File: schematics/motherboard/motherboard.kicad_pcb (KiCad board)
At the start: 2 copper layers, 75 x 43 mm, 2 parts, among them J1 BATTERY, U1 Raspberry_Pi_Pico

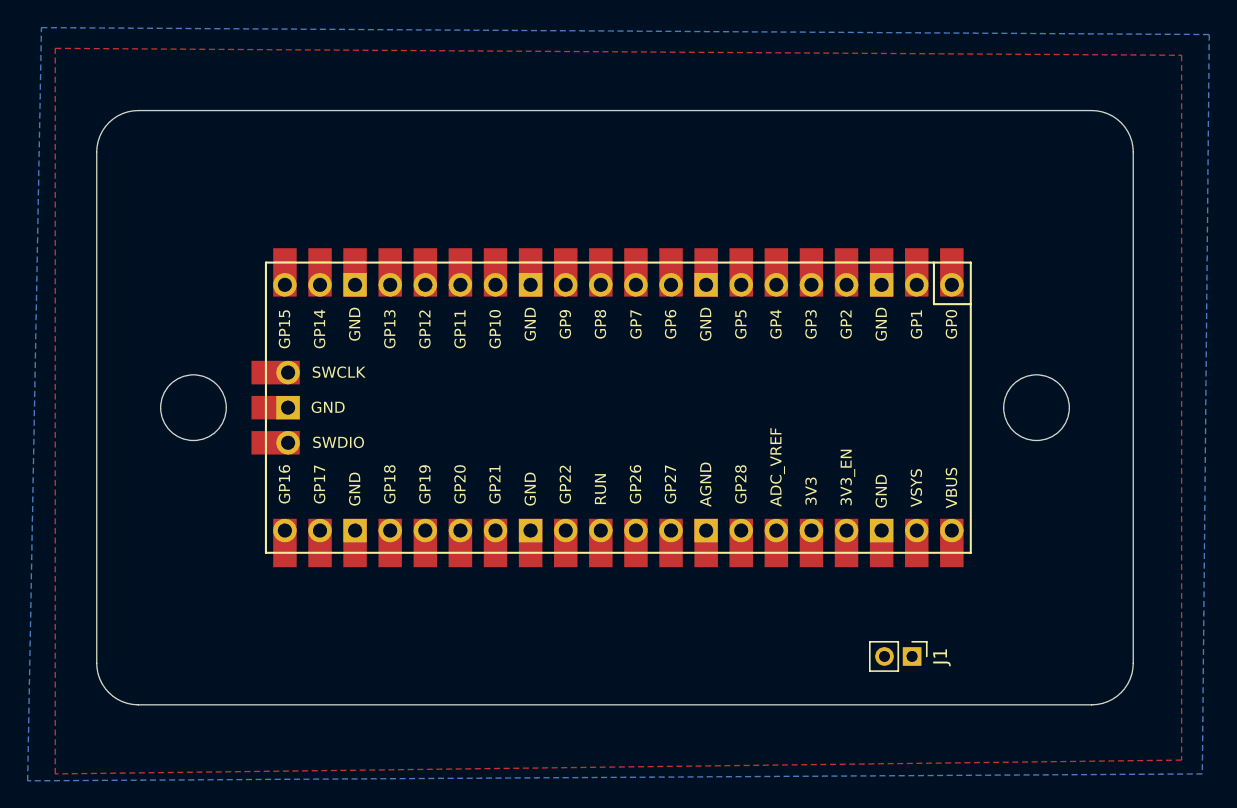
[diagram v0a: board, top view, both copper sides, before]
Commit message: Update fret_board, motherboard and strum_bar schematics
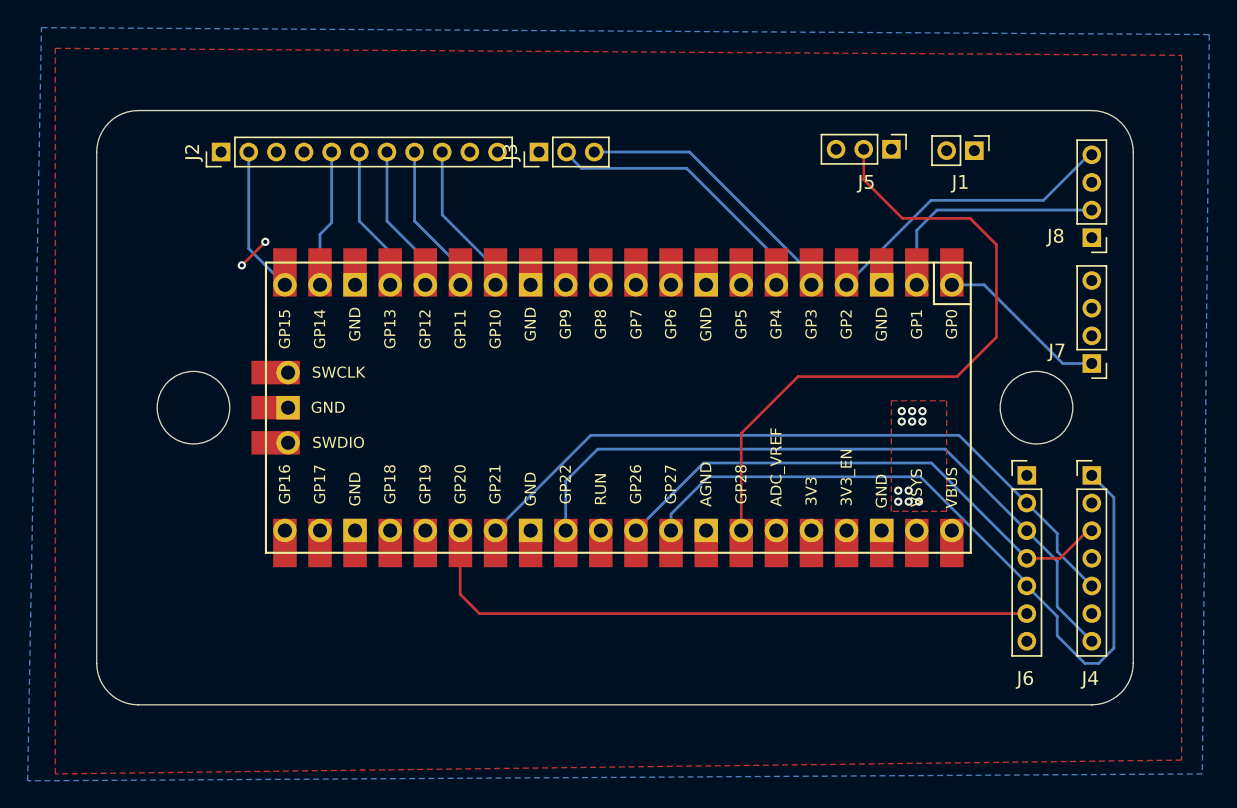
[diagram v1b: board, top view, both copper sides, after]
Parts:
- added J2: NECK, Connector_PinHeader_2.00mm:PinHeader_1x11_P2.00mm_Vertical, F.Cu at (168.0, 51.0)
- added J3: STRUM, Connector_PinHeader_2.00mm:PinHeader_1x03_P2.00mm_Vertical, F.Cu at (191.0, 51.0)
- added J4: DPAD_XBOX, Connector_PinHeader_2.00mm:PinHeader_1x07_P2.00mm_Vertical, F.Cu at (231.0, 74.4)
- added J5: WHAMMY, Connector_PinHeader_2.00mm:PinHeader_1x03_P2.00mm_Vertical, F.Cu at (216.5, 50.8)
- added J6: DPAD_PS2, Connector_PinHeader_2.00mm:PinHeader_1x07_P2.00mm_Vertical, F.Cu at (226.3, 74.4)
- added J7: PAIRING_BTN_XBOX, Connector_PinHeader_2.00mm:PinHeader_1x04_P2.00mm_Vertical, F.Cu at (231.0, 66.3)
- added J8: START_SELECT, Connector_PinHeader_2.00mm:PinHeader_1x04_P2.00mm_Vertical, F.Cu at (231.0, 57.2)
- moved J1 36.9 mm to (222.5, 50.9)
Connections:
- U1 pad 1: unconnected-(U1-GPIO0-Pad1) -> BTN_PAIRING
- U1 pad 14: unconnected-(U1-GPIO10-Pad14) -> FRET_ORANGE
- U1 pad 15: unconnected-(U1-GPIO11-Pad15) -> FRET_BLUE
- U1 pad 16: unconnected-(U1-GPIO12-Pad16) -> FRET_YELLOW
- U1 pad 17: unconnected-(U1-GPIO13-Pad17) -> FRET_RED
- U1 pad 19: unconnected-(U1-GPIO14-Pad19) -> FRET_GREEN
- U1 pad 2: unconnected-(U1-GPIO1-Pad2) -> BTN_START
- U1 pad 20: unconnected-(U1-GPIO15-Pad20) -> NECK_SLIDER
- U1 pad 26: unconnected-(U1-GPIO20-Pad26) -> PS2_LED
- U1 pad 27: unconnected-(U1-GPIO21-Pad27) -> DPAD_UP
- U1 pad 29: unconnected-(U1-GPIO22-Pad29) -> DPAD_DOWN
- U1 pad 31: unconnected-(U1-GPIO26_ADC0-Pad31) -> DPAD_LEFT
- U1 pad 32: unconnected-(U1-GPIO27_ADC1-Pad32) -> DPAD_RIGHT
- U1 pad 34: unconnected-(U1-GPIO28_ADC2-Pad34) -> WHAMMY
- U1 pad 4: unconnected-(U1-GPIO2-Pad4) -> BTN_SELECT
- U1 pad 5: unconnected-(U1-GPIO3-Pad5) -> STRUM_UP
- U1 pad 6: unconnected-(U1-GPIO4-Pad6) -> STRUM_DOWN
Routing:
- net DPAD_RIGHT: track 0.00 -> 54.5 mm
- net DPAD_UP: track 0.00 -> 51.3 mm
- net DPAD_DOWN: track 0.00 -> 50.3 mm
- net WHAMMY: track 0.00 -> 48.8 mm
- net PS2_LED: track 0.00 -> 46.2 mm
- net DPAD_LEFT: track 0.00 -> 38.7 mm
- net BTN_SELECT: track 0.00 -> 21.6 mm
- net STRUM_DOWN: track 0.00 -> 20.3 mm
- net STRUM_UP: track 0.00 -> 20.2 mm
- net BTN_START: track 0.00 -> 17.2 mm
- net BTN_PAIRING: track 0.00 -> 12.5 mm
- net FRET_ORANGE: track 0.00 -> 11.2 mm
- net FRET_BLUE: track 0.00 -> 11.0 mm
- net FRET_YELLOW: track 0.00 -> 10.8 mm
- net NECK_SLIDER: track 0.00 -> 10.7 mm
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- added copper zone on F.Cu, net VCC
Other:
- outline, holes or cut-outs redrawn

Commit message: Add battery sensing circuit and reverse polarity protection diode
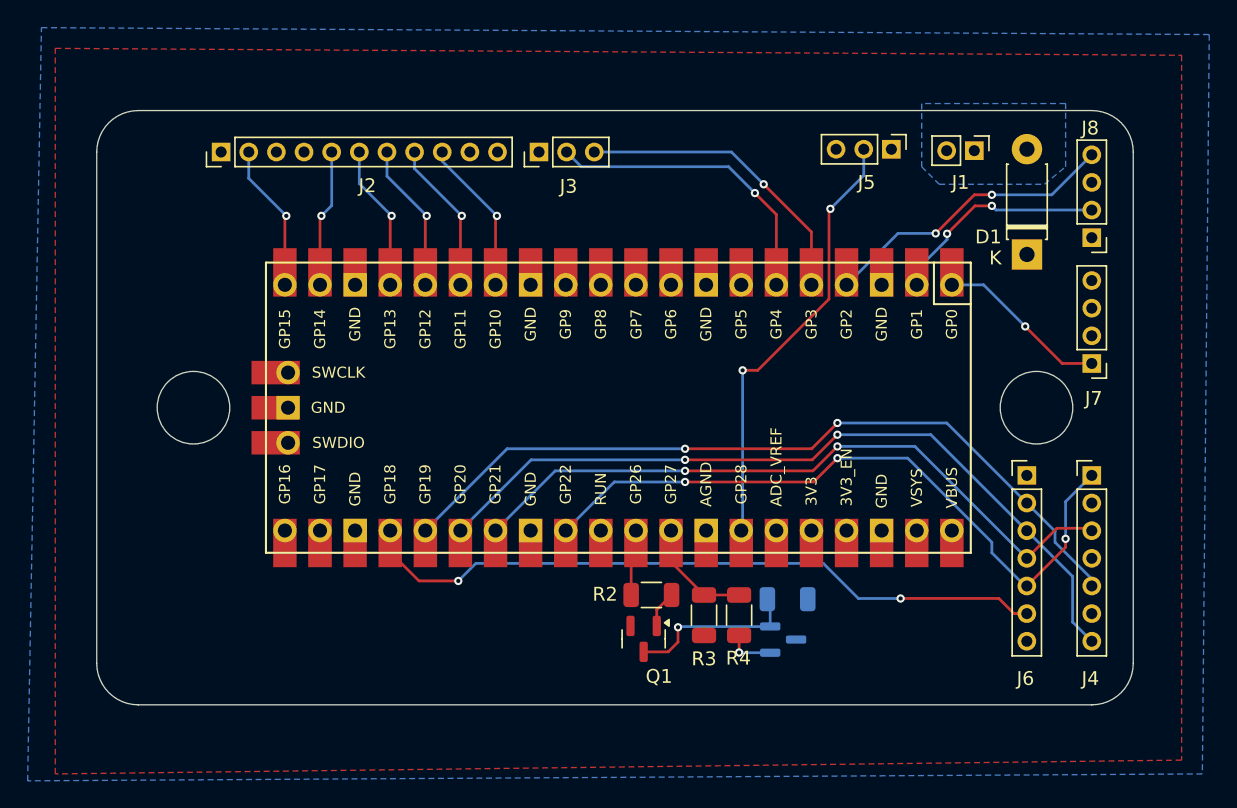
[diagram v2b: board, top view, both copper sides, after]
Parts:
- added D1: 1N5817, Diode_THT:D_DO-41_SOD81_P7.62mm_Horizontal, F.Cu at (226.3, 58.4)
- added Q1: BC847, Package_TO_SOT_SMD:SOT-23, F.Cu at (198.6, 86.2)
- added Q2: IRF5305, Package_TO_SOT_SMD:SOT-23, B.Cu at (208.7, 86.3)
- added R1: 100k, Resistor_SMD:R_1206_3216Metric, B.Cu at (209.0, 83.4)
- added R2: 100k, Resistor_SMD:R_1206_3216Metric, F.Cu at (199.1, 83.1)
- added R3: 100k, Resistor_SMD:R_1206_3216Metric, F.Cu at (205.5, 84.5)
- added R4: 330k, Resistor_SMD:R_1206_3216Metric, F.Cu at (202.9, 84.5)
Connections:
- J1 pad 1: VCC -> /VBAT
- U1 pad 24: unconnected-(U1-GPIO18-Pad24) -> PS2_LED
- U1 pad 25: unconnected-(U1-GPIO19-Pad25) -> DPAD_UP
- U1 pad 26: PS2_LED -> DPAD_DOWN
- U1 pad 27: DPAD_UP -> DPAD_LEFT
- U1 pad 29: DPAD_DOWN -> DPAD_RIGHT
- U1 pad 31: DPAD_LEFT -> VBAT_SENSE_SWITCH
- U1 pad 32: DPAD_RIGHT -> VBAT_SENSE
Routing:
- net WHAMMY: track 48.8 -> 31.9 mm, vias 0 -> 2
- net Net-(Q1-C): track 0.00 -> 12.6 mm, vias 0 -> 1
- net DPAD_LEFT: track 38.7 -> 50.0 mm, vias 0 -> 2
- net VBAT_SENSE: track 0.00 -> 8.19 mm
- net DPAD_DOWN: track 50.3 -> 56.7 mm, vias 0 -> 2
- net DPAD_UP: track 51.3 -> 57.1 mm, vias 0 -> 2
- net VBAT_SENSE_SWITCH: track 0.00 -> 4.81 mm
- net DPAD_RIGHT: track 54.5 -> 49.8 mm, vias 0 -> 3
- net PS2_LED: track 46.2 -> 50.5 mm, vias 0 -> 2
- net Net-(Q2-D): track 0.00 -> 3.49 mm, vias 0 -> 1
- net Net-(Q1-B): track 0.00 -> 2.68 mm
- net VCC: track 2.40 -> 0.00 mm, vias 13 -> 0
- net STRUM_DOWN: track 20.3 -> 22.1 mm, vias 0 -> 1
- net STRUM_UP: track 20.2 -> 21.9 mm, vias 0 -> 1
- net BTN_START: track 17.2 -> 16.0 mm, vias 0 -> 2
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- added copper zone on B.Cu, net /VBAT
- removed copper zone on F.Cu, net VCC

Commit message: Add silkscreen graphics to each schematic
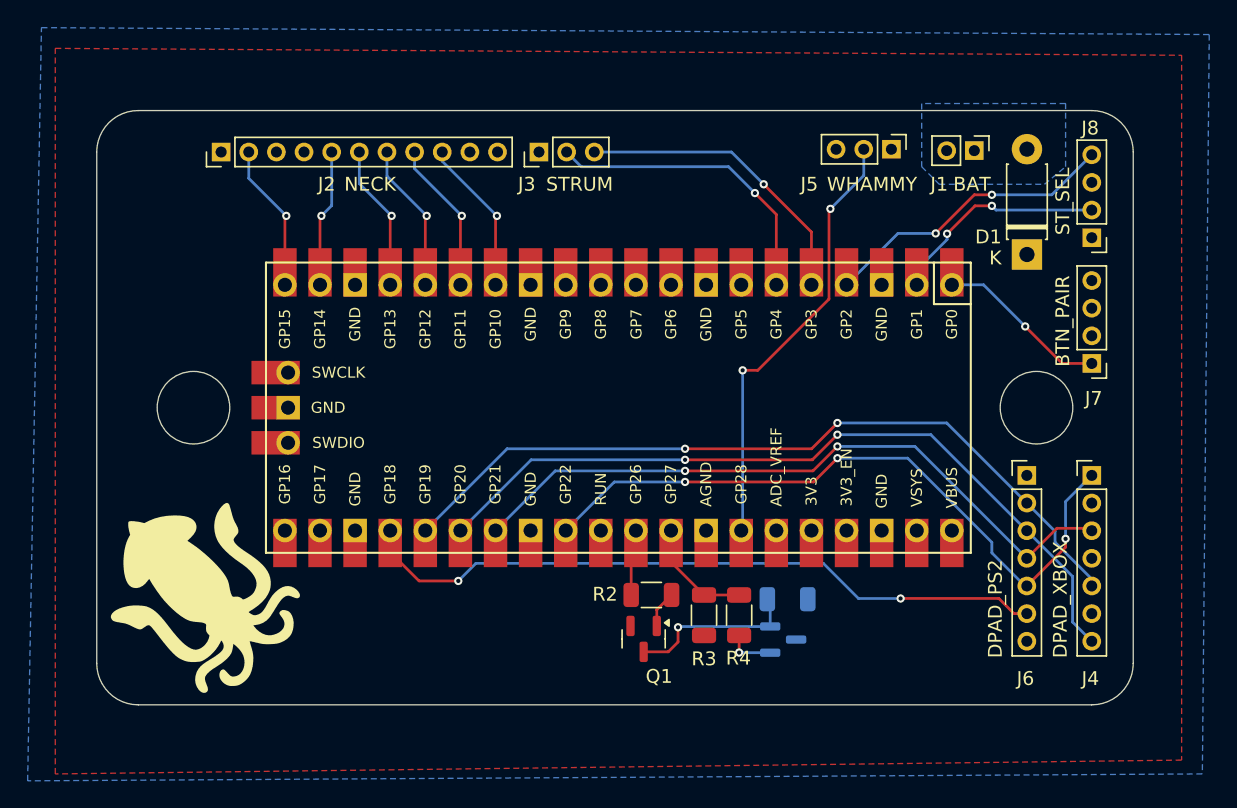
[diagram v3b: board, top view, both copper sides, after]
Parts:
- added G***: LOGO, LOGO, F.Cu at (166.9, 83.3)
- J1: value BATTERY -> BAT
- J8: value START_SELECT -> ST_SEL
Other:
- board text added: "BAT"
- board text added: "BTN_PAIR"
- board text added: "DPAD_PS2"
- board text added: "DPAD_XBOX"
- board text added: "NECK"
- board text added: "STRUM"
- board text added: "ST_SEL"
- board text added: "WHAMMY"

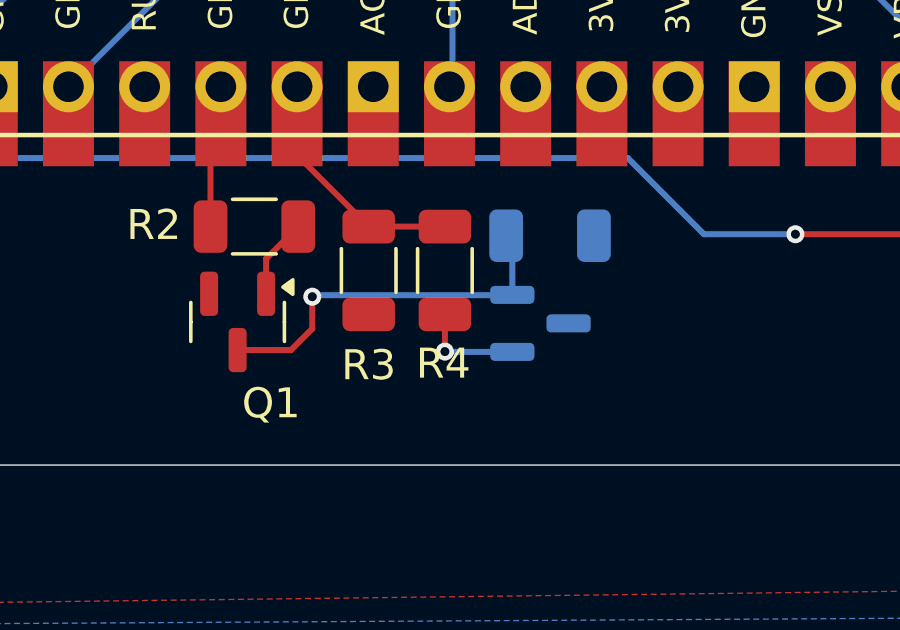
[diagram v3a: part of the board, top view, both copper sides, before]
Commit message: Update Q2 to proper footprint and fix wrong R3/R4 silkscreen
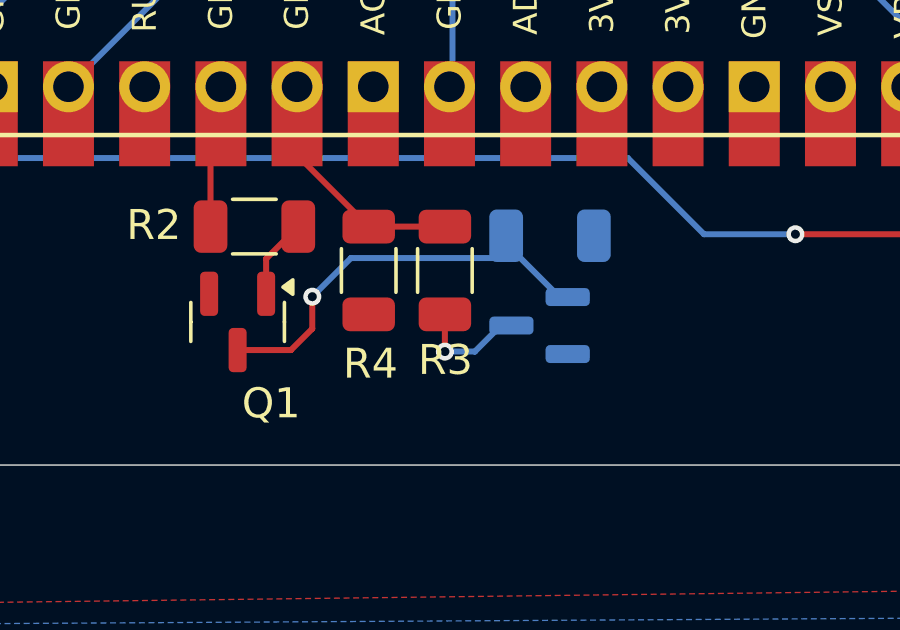
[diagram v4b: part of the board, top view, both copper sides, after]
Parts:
- Q2: value IRF5305 -> BSS84
- moved Q2 0.08 mm to (208.6, 86.3), turned to 180 degrees
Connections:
- Q2 pad 1: Net-(Q2-D) -> Net-(Q1-C)
- Q2 pad 2: Net-(Q1-C) -> VCC
- Q2 pad 3: VCC -> Net-(Q2-D)
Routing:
- net Net-(Q1-C): track 12.6 -> 14.6 mm
